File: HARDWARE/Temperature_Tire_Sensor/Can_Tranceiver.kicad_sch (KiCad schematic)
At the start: 2 parts

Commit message: A completed schematic
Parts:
- removed Z?: PESD2CAN,215, SOT95P230X110-3N, symbol PESD2CAN_215:PESD2CAN,215
- added D?: PESD2CAN,215, symbol Power_Protection:NUP2105L
- added R?: 120, symbol Device:R_US
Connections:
- net GND: now also D?.3 (A)
- net CANH renamed CAN+
- net CAN+: now also D?.2 (K), R?.2
- net CANL renamed CAN-
- net CAN-: now also D?.1 (K), R?.1
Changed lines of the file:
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@@
     (stroke (width 0) (type default) (color 0 0 0 0))
   )
-  (wire (pts (xy 123.19 91.44) (xy 137.16 91.44))
+  (wire (pts (xy 123.19 91.44) (xy 125.73 91.44))
     (stroke (width 0) (type default) (color 0 0 0 0))
   )
-  (wire (pts (xy 123.19 88.9) (xy 137.16 88.9))
+  (wire (pts (xy 147.32 109.22) (xy 147.32 111.76))
+    (stroke (width 0) (type default) (color 0 0 0 0))
+  )
+  (wire (pts (xy 149.86 121.92) (xy 149.86 123.19))
+    (stroke (width 0) (type default) (color 0 0 0 0))
+  )
+  (wire (pts (xy 123.19 88.9) (xy 125.73 88.9))
+    (stroke (width 0) (type default) (color 0 0 0 0))
+  )
+  (wire (pts (xy 152.4 91.44) (xy 158.75 91.44))
+    (stroke (width 0) (type default) (color 0 0 0 0))
+  )
+  (wire (pts (xy 152.4 87.63) (xy 158.75 87.63))
+    (stroke (width 0) (type default) (color 0 0 0 0))
+  )
+  (wire (pts (xy 152.4 109.22) (xy 152.4 111.76))
     (stroke (width 0) (type default) (color 0 0 0 0))
   )
@@
     (stroke (width 0) (type default) (color 0 0 0 0))
   )
-  (wire (pts (xy 139.7 114.3) (xy 139.7 116.84))
+  (wire (pts (xy 128.27 120.65) (xy 128.27 123.19))
     (stroke (width 0) (type default) (color 0 0 0 0))
   )
-  (text "loopback??\nCapacitor 3V3??" (at 104.14 62.23 0)
+  (wire (pts (xy 128.27 110.49) (xy 128.27 113.03))
+    (stroke (width 0) (type default) (color 0 0 0 0))
+  )
+  (text "loopback??\nCapacitor 3V3??" (at 123.19 67.31 0)
     (effects (font (size 1.27 1.27)) (justify left bottom))
   )
-  (label "CAN+" (at 91.44 114.3 180)
-    (effects (font (size 1.27 1.27)) (justify right bottom))
+  (global_label "CAN+" (shape input) (at 125.73 88.9 0) (fields_autoplaced)
+    (effects (font (size 1.27 1.27)) (justify left))
+    (property "Intersheet References" "${INTERSHEET_REFS}" (id 0) (at 133.4045 88.8206 0)
+      (effects (font (size 1.27 1.27)) (justify left) hide)
+    )
   )
-  (label "CAN-" (at 91.44 116.84 180)
-    (effects (font (size 1.27 1.27)) (justify right bottom))
+  (global_label "CAN+" (shape input) (at 128.27 123.19 270) (fields_autoplaced)
+    (effects (font (size 1.27 1.27)) (justify right))
+    (property "Intersheet References" "${INTERSHEET_REFS}" (id 0) (at 128.1906 130.8645 90)
+      (effects (font (size 1.27 1.27)) (justify right) hide)
+    )
   )
-  (label "CAN+" (at 128.27 88.9 0)
-    (effects (font (size 1.27 1.27)) (justify left bottom))
+  (global_label "CAN-" (shape input) (at 152.4 91.44 180) (fields_autoplaced)
+    (effects (font (size 1.27 1.27)) (justify right))
+    (property "Intersheet References" "${INTERSHEET_REFS}" (id 0) (at 144.7255 91.3606 0)
+      (effects (font (size 1.27 1.27)) (justify right) hide)
+    )
   )
-  (label "CAN-" (at 128.27 91.44 0)
-    (effects (font (size 1.27 1.27)) (justify left bottom))
+  (global_label "CAN+" (shape input) (at 152.4 109.22 90) (fields_autoplaced)
+    (effects (font (size 1.27 1.27)) (justify left))
+    (property "Intersheet References" "${INTERSHEET_REFS}" (id 0) (at 152.4794 101.5455 90)
+      (effects (font (size 1.27 1.27)) (justify left) hide)
+    )
   )
-  (hierarchical_label "CANL" (shape bidirectional) (at 137.16 91.44 0)
+  (global_label "CAN+" (shape input) (at 152.4 87.63 180) (fields_autoplaced)
+    (effects (font (size 1.27 1.27)) (justify right))
+    (property "Intersheet References" "${INTERSHEET_REFS}" (id 0) (at 144.7255 87.5506 0)
+      (effects (font (size 1.27 1.27)) (justify right) hide)
+    )
+  )
+  (global_label "CAN-" (shape input) (at 147.32 109.22 90) (fields_autoplaced)
+    (effects (font (size 1.27 1.27)) (justify left))
+    (property "Intersheet References" "${INTERSHEET_REFS}" (id 0) (at 147.3994 101.5455 90)
+      (effects (font (size 1.27 1.27)) (justify left) hide)
+    )
+  )
+  (global_label "CAN-" (shape input) (at 128.27 110.49 90) (fields_autoplaced)
+    (effects (font (size 1.27 1.27)) (justify left))
+    (property "Intersheet References" "${INTERSHEET_REFS}" (id 0) (at 128.1906 102.8155 90)
+      (effects (font (size 1.27 1.27)) (justify left) hide)
+    )
+  )
+  (global_label "CAN-" (shape input) (at 125.73 91.44 0) (fields_autoplaced)
+    (effects (font (size 1.27 1.27)) (justify left))
+    (property "Intersheet References" "${INTERSHEET_REFS}" (id 0) (at 133.4045 91.3606 0)
+      (effects (font (size 1.27 1.27)) (justify left) hide)
+    )
+  )
+  (hierarchical_label "CANH" (shape bidirectional) (at 158.75 87.63 0)
+    (effects (font (size 1.27 1.27)) (justify left))
+  )
+  (hierarchical_label "CANL" (shape bidirectional) (at 158.75 91.44 0)
     (effects (font (size 1.27 1.27)) (justify left))
   )
@@
     (effects (font (size 1.27 1.27)) (justify right))
   )
-  (hierarchical_label "CANH" (shape bidirectional) (at 137.16 88.9 0)
-    (effects (font (size 1.27 1.27)) (justify left))
-  )
-  (symbol (lib_id "PESD2CAN_215:PESD2CAN,215") (at 91.44 114.3 0) (unit 1)
+  (symbol (lib_id "Power_Protection:NUP2105L") (at 149.86 116.84 0) (unit 1)
     (in_bom yes) (on_board yes) (fields_autoplaced)
-    (property "Reference" "Z?" (id 0) (at 115.57 106.68 0))
-    (property "Value" "PESD2CAN,215" (id 1) (at 115.57 109.22 0))
-    (property "Footprint" "SOT95P230X110-3N" (id 2) (at 135.89 111.76 0)
+    (property "Reference" "D?" (id 0) (at 156.21 115.5699 0)
+      (effects (font (size 1.27 1.27)) (justify left))
+    )
+    (property "Value" "PESD2CAN,215" (id 1) (at 156.21 118.1099 0)
+      (effects (font (size 1.27 1.27)) (justify left))
+    )
+    (property "Footprint" "" (id 2) (at 155.575 118.11 0)
       (effects (font (size 1.27 1.27)) (justify left) hide)
     )
-    (property "Datasheet" "https://datasheet.datasheetarchive.com/originals/distributors/Datasheets_SAMA/5df5edafdc67e6ae251d12d61f18e7bd.pdf" (id 3) (at 135.89 114.3 0)
-      (effects (font (size 1.27 1.27)) (justify left) hide)
+    (property "Datasheet" "" (id 3) (at 153.035 113.665 0)
+      (effects (font (size 1.27 1.27)) hide)
     )
-    (property "Description" "NXP PESD2CAN,215 Dual Bi-Directional ESD Protection Diode, 230W peak, 3-Pin SOT23 (TO-236AB)" (id 4) (at 135.89 116.84 0)
-      (effects (font (size 1.27 1.27)) (justify left) hide)
-    )
-    (property "Height" "1.1" (id 5) (at 135.89 119.38 0)
-      (effects (font (size 1.27 1.27)) (justify left) hide)
-    )
-    (property "Manufacturer_Name" "Nexperia" (id 6) (at 135.89 121.92 0)
-      (effects (font (size 1.27 1.27)) (justify left) hide)
-    )
-    (property "Manufacturer_Part_Number" "PESD2CAN,215" (id 7) (at 135.89 124.46 0)
-      (effects (font (size 1.27 1.27)) (justify left) hide)
-    )
-    (property "Mouser Part Number" "771-PESD2CAN-T/R" (id 8) (at 135.89 127 0)
-      (effects (font (size 1.27 1.27)) (justify left) hide)
-    )
-    (property "Mouser Price/Stock" "https://www.mouser.co.uk/ProductDetail/Nexperia/PESD2CAN215?qs=LOCUfHb8d9sqg7TaLUP2JQ%3D%3D" (id 9) (at 135.89 129.54 0)
-      (effects (font (size 1.27 1.27)) (justify left) hide)
-    )
-    (property "Arrow Part Number" "PESD2CAN,215" (id 10) (at 135.89 132.08 0)
-      (effects (font (size 1.27 1.27)) (justify left) hide)
-    )
-    (property "Arrow Price/Stock" "https://www.arrow.com/en/products/pesd2can215/nexperia?region=nac" (id 11) (at 135.89 134.62 0)
-      (effects (font (size 1.27 1.27)) (justify left) hide)
-    )
+    (pin "3")
     (pin "1")
     (pin "2")
-    (pin "3")
   )
   (symbol (lib_id "power:GND") (at 113.03 100.33 0) (unit 1)
-    (in_bom yes) (on_board yes) (fields_autoplaced)
+    (in_bom yes) (on_board yes)
     (property "Reference" "#PWR?" (id 0) (at 113.03 106.68 0)
       (effects (font (size 1.27 1.27)) hide)
     )
-    (property "Value" "~" (id 1) (at 113.03 105.41 0))
+    (property "Value" "~" (id 1) (at 119.38 111.76 0))
     (property "Footprint" "" (id 2) (at 113.03 100.33 0)
       (effects (font (size 1.27 1.27)) hide)
@@
     (pin "1")
   )
-  (symbol (lib_id "power:GND") (at 139.7 116.84 0) (unit 1)
+  (symbol (lib_id "power:GND") (at 149.86 123.19 0) (unit 1)
     (in_bom yes) (on_board yes) (fields_autoplaced)
-    (property "Reference" "#PWR?" (id 0) (at 139.7 123.19 0)
+    (property "Reference" "#PWR?" (id 0) (at 149.86 129.54 0)
       (effects (font (size 1.27 1.27)) hide)
     )
-    (property "Value" "GND" (id 1) (at 139.7 121.92 0))
-    (property "Footprint" "" (id 2) (at 139.7 116.84 0)
+    (property "Value" "GND" (id 1) (at 149.86 128.27 0))
+    (property "Footprint" "" (id 2) (at 149.86 123.19 0)
       (effects (font (size 1.27 1.27)) hide)
     )
-    (property "Datasheet" "" (id 3) (at 139.7 116.84 0)
+    (property "Datasheet" "" (id 3) (at 149.86 123.19 0)
       (effects (font (size 1.27 1.27)) hide)
     )
@@
     (pin "1")
   )
+  (symbol (lib_id "Device:R_US") (at 128.27 116.84 0) (unit 1)
+    (in_bom yes) (on_board yes) (fields_autoplaced)
+    (property "Reference" "R?" (id 0) (at 130.81 115.5699 0)
+      (effects (font (size 1.27 1.27)) (justify left))
+    )
+    (property "Value" "120" (id 1) (at 130.81 118.1099 0)
+      (effects (font (size 1.27 1.27)) (justify left))
+    )
+    (property "Footprint" "" (id 2) (at 129.286 117.094 90)
+      (effects (font (size 1.27 1.27)) hide)
+    )
+    (property "Datasheet" "~" (id 3) (at 128.27 116.84 0)
+      (effects (font (size 1.27 1.27)) hide)
+    )
+    (pin "1")
+    (pin "2")
+  )
   (symbol (lib_id "Interface_CAN_LIN:SN65HVD232") (at 113.03 88.9 0) (unit 1)

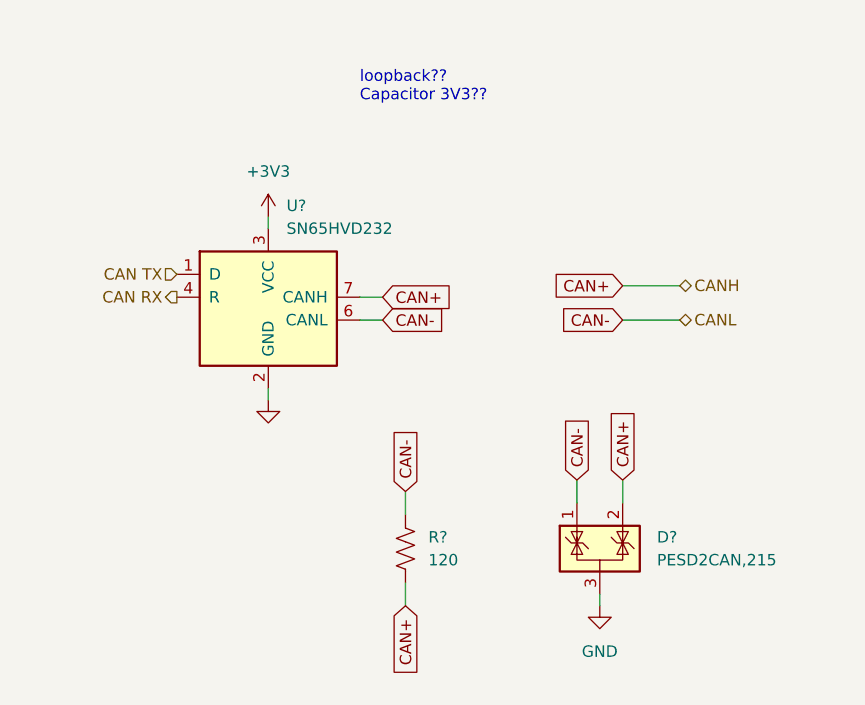
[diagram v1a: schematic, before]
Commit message: Changed the used type of labels and added power flags
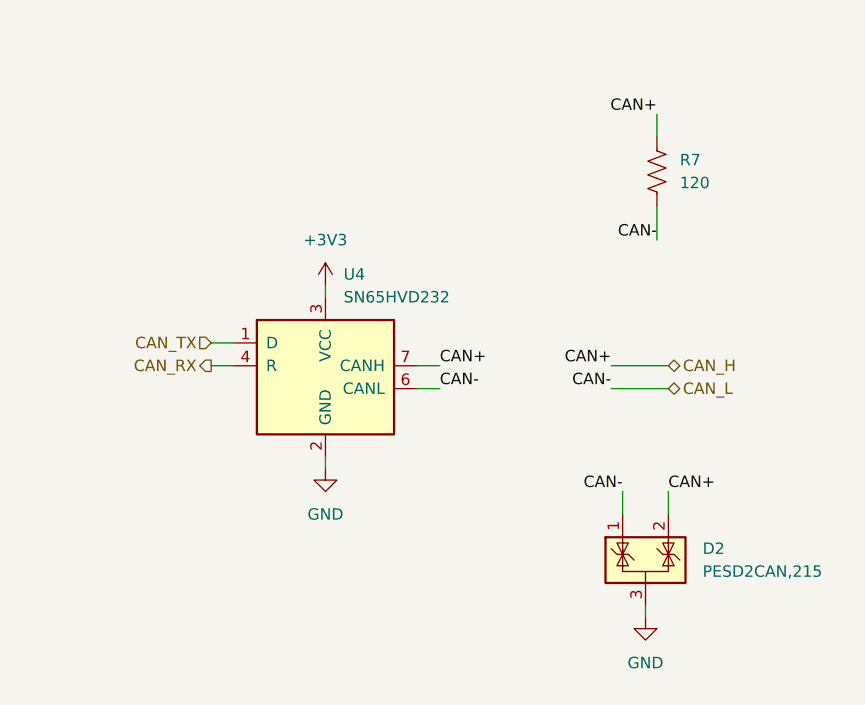
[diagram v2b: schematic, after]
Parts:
- gave numbers to parts that had none: 3
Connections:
- net CAN RX renamed CAN_RX
- net CAN TX renamed CAN_TX
- net CAN+ renamed CAN_H
- net CAN_H: now also R7.1; no longer R7.2
- net CAN- renamed CAN_L
- net CAN_L: now also R7.2; no longer R7.1
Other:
- note removed: "loopback?? Capacitor 3V3??"
- moved on the sheet: D2, R7, U4

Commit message: Added all of the footprints
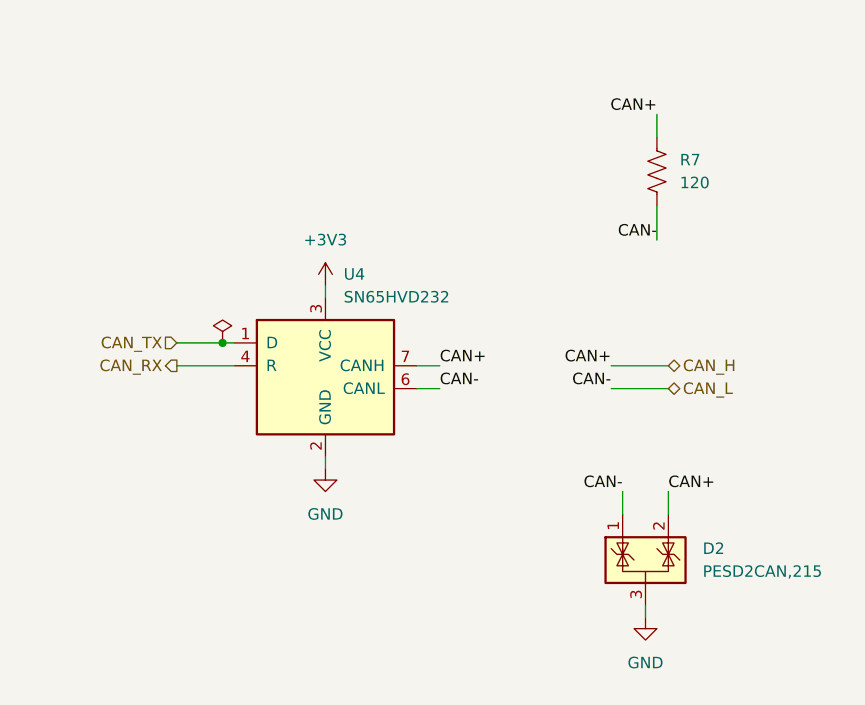
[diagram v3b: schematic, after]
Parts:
- D2: footprint (none) -> TSOT23-5:SOT-23
- R7: footprint (none) -> Resistor_SMD:R_0603_1608Metric
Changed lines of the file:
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@@
 (kicad_sch (version 20211123) (generator eeschema)
   (paper "A4")
+  (junction (at 107.95 93.98) (diameter 0) (color 0 0 0 0)
+  )
   (wire (pts (xy 119.38 87.63) (xy 119.38 88.9))
     (stroke (width 0) (type default) (color 0 0 0 0))
@@
     (stroke (width 0) (type default) (color 0 0 0 0))
   )
+  (wire (pts (xy 102.87 93.98) (xy 107.95 93.98))
+    (stroke (width 0) (type default) (color 0 0 0 0))
+  )
+  (wire (pts (xy 107.95 93.98) (xy 109.22 93.98))
+    (stroke (width 0) (type default) (color 0 0 0 0))
+  )
   (wire (pts (xy 156.21 68.58) (xy 156.21 71.12))
     (stroke (width 0) (type default) (color 0 0 0 0))
   )
-  (wire (pts (xy 106.68 96.52) (xy 109.22 96.52))
-    (stroke (width 0) (type default) (color 0 0 0 0))
-  )
-  (wire (pts (xy 106.68 93.98) (xy 109.22 93.98))
+  (wire (pts (xy 102.87 96.52) (xy 109.22 96.52))
     (stroke (width 0) (type default) (color 0 0 0 0))
   )
@@
     (effects (font (size 1.27 1.27)) (justify left))
   )
-  (hierarchical_label "CAN_RX" (shape output) (at 106.68 96.52 180)
+  (hierarchical_label "CAN_RX" (shape output) (at 102.87 96.52 180)
     (effects (font (size 1.27 1.27)) (justify right))
   )
-  (hierarchical_label "CAN_TX" (shape input) (at 106.68 93.98 180)
+  (hierarchical_label "CAN_TX" (shape input) (at 102.87 93.98 180)
     (effects (font (size 1.27 1.27)) (justify right))
   )
@@
       (effects (font (size 1.27 1.27)) (justify left))
     )
-    (property "Footprint" "" (id 2) (at 160.655 119.38 0)
+    (property "Footprint" "TSOT23-5:SOT-23" (id 2) (at 160.655 119.38 0)
       (effects (font (size 1.27 1.27)) (justify left) hide)
     )
@@
     (pin "1")
     (pin "2")
+  )
+  (symbol (lib_id "power:PWR_FLAG") (at 107.95 93.98 0) (unit 1)
+    (in_bom yes) (on_board yes) (fields_autoplaced)
+    (property "Reference" "#FLG01" (id 0) (at 107.95 92.075 0)
+      (effects (font (size 1.27 1.27)) hide)
+    )
+    (property "Value" "PWR_FLAG" (id 1) (at 107.95 88.9 0)
+      (effects (font (size 1.27 1.27)) hide)
+    )
+    (property "Footprint" "" (id 2) (at 107.95 93.98 0)
+      (effects (font (size 1.27 1.27)) hide)
+    )
+    (property "Datasheet" "~" (id 3) (at 107.95 93.98 0)
+      (effects (font (size 1.27 1.27)) hide)
+    )
+    (pin "1")
   )
   (symbol (lib_id "power:GND") (at 154.94 124.46 0) (unit 1)
@@
       (effects (font (size 1.27 1.27)) (justify left))
     )
-    (property "Footprint" "" (id 2) (at 157.226 75.184 90)
+    (property "Footprint" "Resistor_SMD:R_0603_1608Metric" (id 2) (at 157.226 75.184 90)
       (effects (font (size 1.27 1.27)) hide)
     )

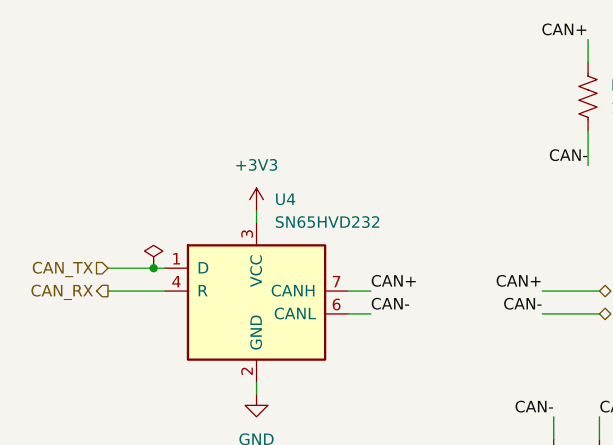
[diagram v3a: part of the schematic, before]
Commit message: Power planes has been added
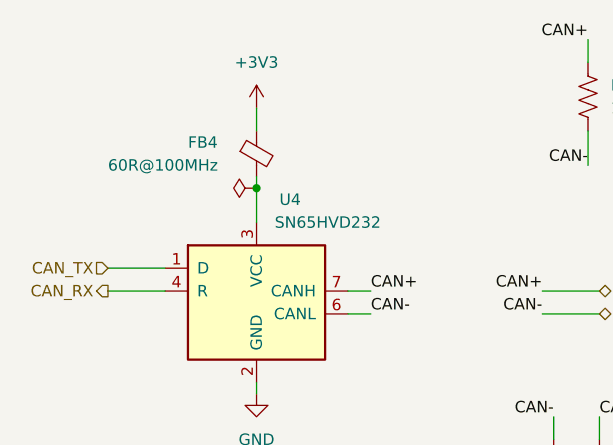
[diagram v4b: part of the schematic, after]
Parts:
- added FB4: 60R@100MHz, Inductor_SMD:L_0603_1608Metric, symbol Device:FerriteBead_Small
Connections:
- net +3V3: now also FB4.1; no longer U4.3 (VCC)
- new net: FB4.2, U4.3 (VCC)
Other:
- title: (none) -> CAN
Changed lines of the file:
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@@
 (kicad_sch (version 20211123) (generator eeschema)
   (paper "A4")
-  (junction (at 107.95 93.98) (diameter 0) (color 0 0 0 0)
-  )
-  (wire (pts (xy 119.38 87.63) (xy 119.38 88.9))
+  (title_block
+    (title "CAN")
+  )
+  (junction (at 119.38 85.09) (diameter 0) (color 0 0 0 0)
+  )
+  (wire (pts (xy 119.38 83.82) (xy 119.38 85.09))
     (stroke (width 0) (type default) (color 0 0 0 0))
   )
@@
     (stroke (width 0) (type default) (color 0 0 0 0))
   )
+  (wire (pts (xy 119.38 76.2) (xy 119.38 78.74))
+    (stroke (width 0) (type default) (color 0 0 0 0))
+  )
   (wire (pts (xy 151.13 96.52) (xy 157.48 96.52))
     (stroke (width 0) (type default) (color 0 0 0 0))
@@
     (stroke (width 0) (type default) (color 0 0 0 0))
   )
-  (wire (pts (xy 102.87 93.98) (xy 107.95 93.98))
-    (stroke (width 0) (type default) (color 0 0 0 0))
-  )
-  (wire (pts (xy 107.95 93.98) (xy 109.22 93.98))
+  (wire (pts (xy 102.87 93.98) (xy 109.22 93.98))
     (stroke (width 0) (type default) (color 0 0 0 0))
   )
@@
   )
   (wire (pts (xy 102.87 96.52) (xy 109.22 96.52))
+    (stroke (width 0) (type default) (color 0 0 0 0))
+  )
+  (wire (pts (xy 119.38 85.09) (xy 119.38 88.9))
     (stroke (width 0) (type default) (color 0 0 0 0))
   )
@@
     (pin "1")
   )
+  (symbol (lib_id "power:+3V3") (at 119.38 76.2 0) (unit 1)
+    (in_bom yes) (on_board yes) (fields_autoplaced)
+    (property "Reference" "#PWR08" (id 0) (at 119.38 80.01 0)
+      (effects (font (size 1.27 1.27)) hide)
+    )
+    (property "Value" "+3V3" (id 1) (at 119.38 71.12 0))
+    (property "Footprint" "" (id 2) (at 119.38 76.2 0)
+      (effects (font (size 1.27 1.27)) hide)
+    )
+    (property "Datasheet" "" (id 3) (at 119.38 76.2 0)
+      (effects (font (size 1.27 1.27)) hide)
+    )
+    (pin "1")
+  )
   (symbol (lib_id "Power_Protection:NUP2105L") (at 154.94 118.11 0) (unit 1)
     (in_bom yes) (on_board yes) (fields_autoplaced)
@@
     (pin "2")
   )
-  (symbol (lib_id "power:PWR_FLAG") (at 107.95 93.98 0) (unit 1)
-    (in_bom yes) (on_board yes) (fields_autoplaced)
-    (property "Reference" "#FLG01" (id 0) (at 107.95 92.075 0)
-      (effects (font (size 1.27 1.27)) hide)
-    )
-    (property "Value" "PWR_FLAG" (id 1) (at 107.95 88.9 0)
-      (effects (font (size 1.27 1.27)) hide)
-    )
-    (property "Footprint" "" (id 2) (at 107.95 93.98 0)
-      (effects (font (size 1.27 1.27)) hide)
-    )
-    (property "Datasheet" "~" (id 3) (at 107.95 93.98 0)
-      (effects (font (size 1.27 1.27)) hide)
-    )
-    (pin "1")
-  )
   (symbol (lib_id "power:GND") (at 154.94 124.46 0) (unit 1)
     (in_bom yes) (on_board yes) (fields_autoplaced)
@@
     (pin "1")
   )
-  (symbol (lib_id "power:+3V3") (at 119.38 87.63 0) (unit 1)
-    (in_bom yes) (on_board yes) (fields_autoplaced)
-    (property "Reference" "#PWR021" (id 0) (at 119.38 91.44 0)
-      (effects (font (size 1.27 1.27)) hide)
-    )
-    (property "Value" "+3V3" (id 1) (at 119.38 82.55 0))
-    (property "Footprint" "" (id 2) (at 119.38 87.63 0)
-      (effects (font (size 1.27 1.27)) hide)
-    )
-    (property "Datasheet" "" (id 3) (at 119.38 87.63 0)
-      (effects (font (size 1.27 1.27)) hide)
-    )
-    (pin "1")
-  )
   (symbol (lib_id "Device:R_US") (at 156.21 74.93 0) (unit 1)
     (in_bom yes) (on_board yes) (fields_autoplaced)
@@
   )
   (symbol (lib_id "Interface_CAN_LIN:SN65HVD232") (at 119.38 96.52 0) (unit 1)
-    (in_bom yes) (on_board yes) (fields_autoplaced)
-    (property "Reference" "U4" (id 0) (at 121.3994 86.36 0)
+    (in_bom yes) (on_board yes)
+    (property "Reference" "U4" (id 0) (at 121.92 86.36 0)
       (effects (font (size 1.27 1.27)) (justify left))
     )
@@
     (pin "8")
   )
+  (symbol (lib_id "power:PWR_FLAG") (at 119.38 85.09 90) (unit 1)
+    (in_bom yes) (on_board yes) (fields_autoplaced)
+    (property "Reference" "#FLG0104" (id 0) (at 117.475 85.09 0)
+      (effects (font (size 1.27 1.27)) hide)
+    )
+    (property "Value" "PWR_FLAG" (id 1) (at 114.3 85.09 0)
+      (effects (font (size 1.27 1.27)) hide)
+    )
+    (property "Footprint" "" (id 2) (at 119.38 85.09 0)
+      (effects (font (size 1.27 1.27)) hide)
+    )
+    (property "Datasheet" "~" (id 3) (at 119.38 85.09 0)
+      (effects (font (size 1.27 1.27)) hide)
+    )
+    (pin "1")
+  )
+  (symbol (lib_id "Device:FerriteBead_Small") (at 119.38 81.28 0) (unit 1)
+    (in_bom yes) (on_board yes)
+    (property "Reference" "FB4" (id 0) (at 111.76 80.01 0)
+      (effects (font (size 1.27 1.27)) (justify left))
+    )
+    (property "Value" "60R@100MHz" (id 1) (at 102.87 82.55 0)
+      (effects (font (size 1.27 1.27)) (justify left))
+    )
+    (property "Footprint" "Inductor_SMD:L_0603_1608Metric" (id 2) (at 117.602 81.28 90)
+      (effects (font (size 1.27 1.27)) hide)
+    )
+    (property "Datasheet" "~" (id 3) (at 119.38 81.28 0)
+      (effects (font (size 1.27 1.27)) hide)
+    )
+    (pin "1")
+    (pin "2")
+  )
 )
